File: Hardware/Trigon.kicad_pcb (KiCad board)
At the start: 2 copper layers, 160 x 120 mm, 110 parts, among them J1 TYPE-C-31-M12_13, J2 TYPE-C-31-M12_13, J3 Conn_01x05, SW1 SW_Push, SW2 Rotary_Encoder_Switch, U1 ATmega32U4-AU, U2 USBLC6-2SC6, U3 CY7C65632-28LTXCT, U4 USBLC6-2SC6, Y1 16MHz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

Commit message: minor tweaks to layout
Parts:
- moved C7 2.87 mm to (138.9, 59.5)
- moved C5 1.12 mm to (151.6, 61.9)
- moved C4 0.79 mm to (154.8, 48.4)
- moved R1 0.38 mm to (135.8, 55.2)
- moved R2 0.38 mm to (135.8, 56.8)
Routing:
- net COL6: track 22.3 -> 26.9 mm
- net D1_D-: track 57.4 -> 61.4 mm
- net GND: track 49.1 -> 46.3 mm
- net +5V: track 286.3 -> 288.7 mm, vias 9 -> 10
- net D1_D+: track 60.0 -> 61.5 mm

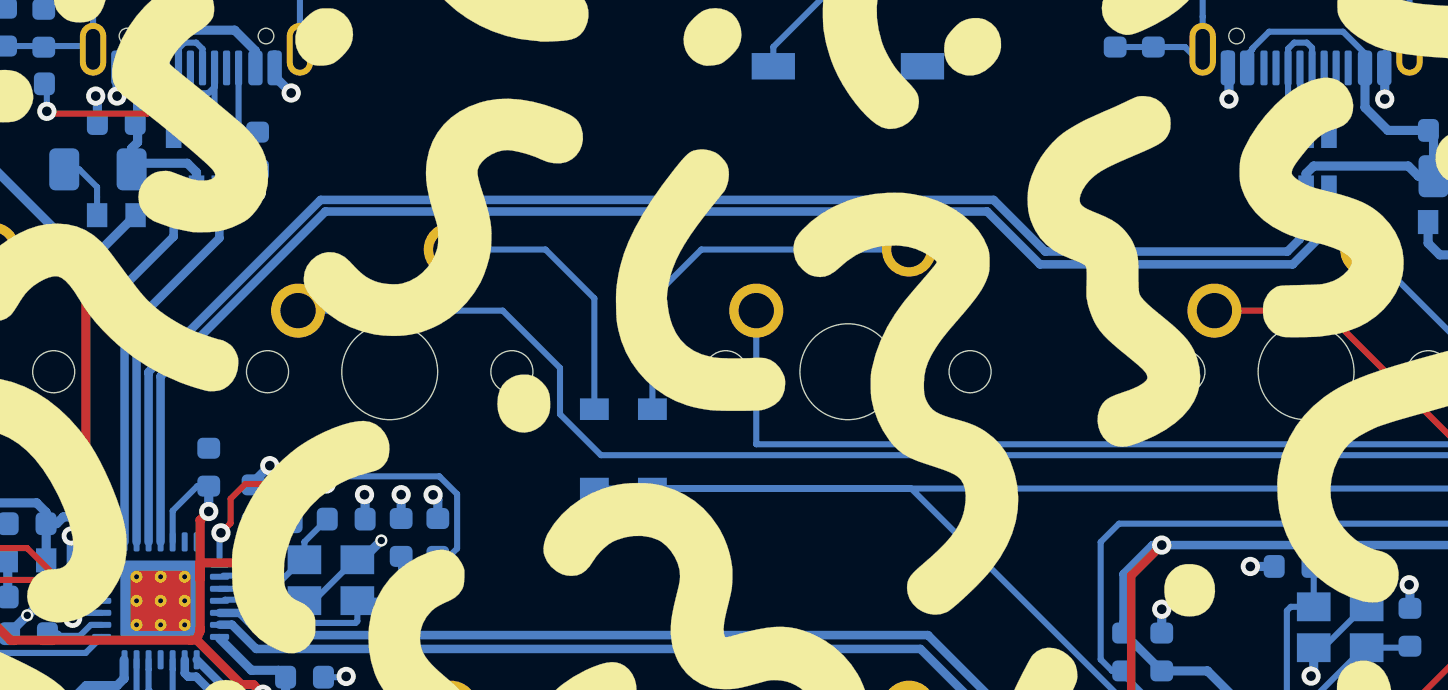
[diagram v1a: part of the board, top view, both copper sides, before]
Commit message: more space for usb
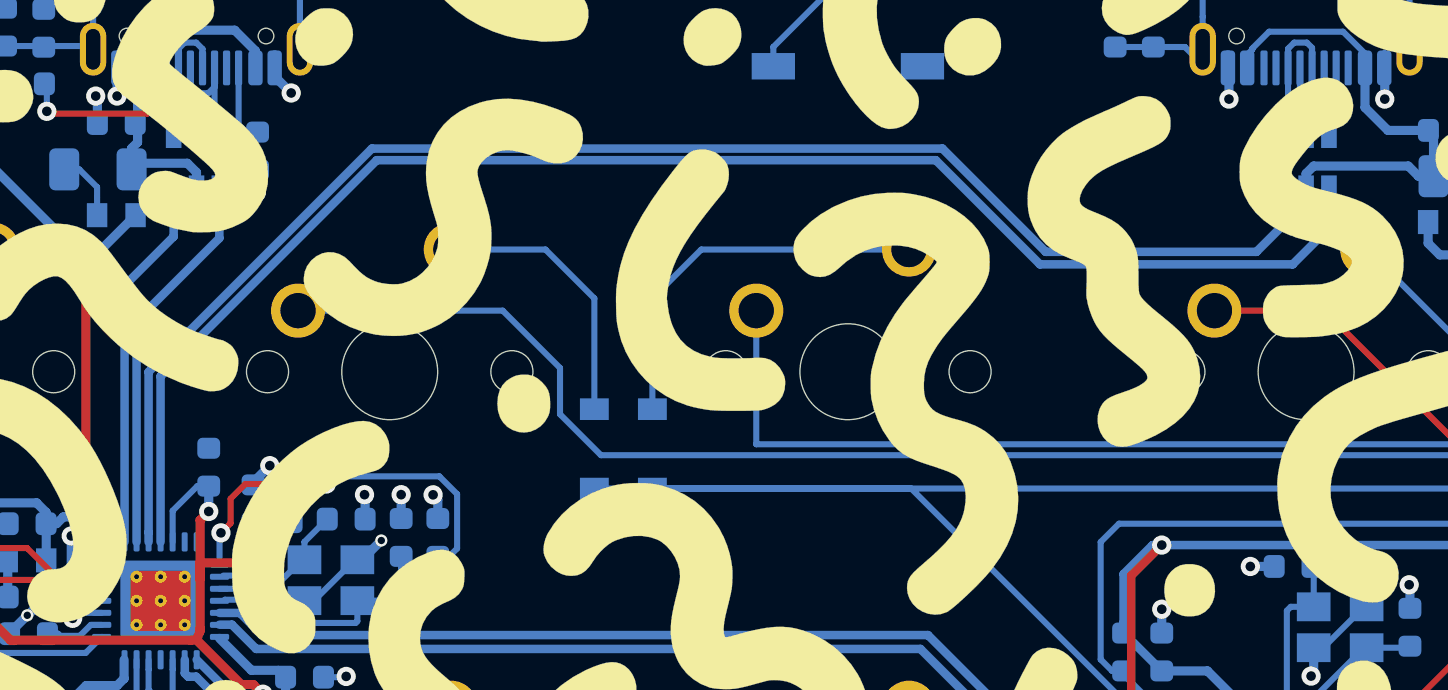
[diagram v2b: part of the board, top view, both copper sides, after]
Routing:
- net D1_D+: track 61.5 -> 63.3 mm
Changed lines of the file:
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@@
     (thickness 1.6)
     (drawings 21)
-    (tracks 814)
+    (tracks 812)
     (zones 0)
     (modules 110)
@@
   (segment (start 98.21875 30.43225) (end 101.661 26.99) (width 0.3556) (layer B.Cu) (net 97))
   (segment (start 98.21875 39.61875) (end 98.21875 30.43225) (width 0.3556) (layer B.Cu) (net 97))
-  (segment (start 146.57705 27.035778) (end 146.066528 27.5463) (width 0.3556) (layer B.Cu) (net 98))
-  (segment (start 98.71875 32.551737) (end 98.71875 32.59925) (width 0.3556) (layer B.Cu) (net 98))
-  (segment (start 98.71875 32.59925) (end 98.71875 39.61875) (width 0.3556) (layer B.Cu) (net 98))
-  (segment (start 146.066528 27.5463) (end 136.000472 27.5463) (width 0.3556) (layer B.Cu) (net 98))
-  (segment (start 105.870487 25.4) (end 98.71875 32.551737) (width 0.3556) (layer B.Cu) (net 98))
-  (segment (start 133.854172 25.4) (end 105.870487 25.4) (width 0.3556) (layer B.Cu) (net 98))
-  (segment (start 145.89375 24.9125) (end 145.89375 25.707501) (width 0.3556) (layer B.Cu) (net 98))
-  (segment (start 136.000472 27.5463) (end 133.854172 25.4) (width 0.3556) (layer B.Cu) (net 98))
-  (segment (start 145.89375 25.707501) (end 146.57705 26.390801) (width 0.3556) (layer B.Cu) (net 98))
-  (segment (start 146.57705 26.390801) (end 146.57705 27.035778) (width 0.3556) (layer B.Cu) (net 98))
-  (segment (start 135.779528 28.0797) (end 133.582439 25.882611) (width 0.3556) (layer B.Cu) (net 99))
+  (segment (start 98.71875 32.551736) (end 98.71875 39.21875) (width 0.3556) (layer B.Cu) (net 98))
+  (segment (start 98.71875 39.21875) (end 98.71875 39.61875) (width 0.3556) (layer B.Cu) (net 98))
+  (segment (start 108.004097 23.266389) (end 98.71875 32.551736) (width 0.3556) (layer B.Cu) (net 98))
+  (segment (start 131.724389 23.266389) (end 108.004097 23.266389) (width 0.3556) (layer B.Cu) (net 98))
+  (segment (start 136.017 27.559) (end 131.724389 23.266389) (width 0.3556) (layer B.Cu) (net 98))
+  (segment (start 145.89375 26.44525) (end 144.78 27.559) (width 0.3556) (layer B.Cu) (net 98))
+  (segment (start 144.78 27.559) (end 136.017 27.559) (width 0.3556) (layer B.Cu) (net 98))
+  (segment (start 145.89375 24.9125) (end 145.89375 26.44525) (width 0.3556) (layer B.Cu) (net 98))
   (segment (start 99.21594 32.737061) (end 99.21594 39.61875) (width 0.3556) (layer B.Cu) (net 99))
-  (segment (start 133.582439 25.882611) (end 106.07039 25.882611) (width 0.3556) (layer B.Cu) (net 99))
+  (segment (start 108.204001 23.749) (end 99.21594 32.737061) (width 0.3556) (layer B.Cu) (net 99))
+  (segment (start 135.779528 28.0797) (end 131.448828 23.749) (width 0.3556) (layer B.Cu) (net 99))
   (segment (start 147.79375 26.573422) (end 146.287472 28.0797) (width 0.3556) (layer B.Cu) (net 99))
   (segment (start 147.79375 24.9125) (end 147.79375 26.573422) (width 0.3556) (layer B.Cu) (net 99))
-  (segment (start 106.07039 25.882611) (end 99.21594 32.737061) (width 0.3556) (layer B.Cu) (net 99))
   (segment (start 146.287472 28.0797) (end 135.779528 28.0797) (width 0.3556) (layer B.Cu) (net 99))
+  (segment (start 131.448828 23.749) (end 108.204001 23.749) (width 0.3556) (layer B.Cu) (net 99))
   (segment (start 97.409 45.593) (end 97.70124 45.30076) (width 0.381) (layer B.Cu) (net 100))
   (segment (start 96.12125 45.593) (end 97.409 45.593) (width 0.381) (layer B.Cu) (net 100))

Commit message: min track width
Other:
- net class Narrow removed
- rule trace_min: 0.1524 -> 0.1778
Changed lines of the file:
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@@
   (setup
     (last_trace_width 0.254)
-    (user_trace_width 0.1524)
     (user_trace_width 0.2032)
     (user_trace_width 0.254)
@@
     (zone_clearance 0.25)
     (zone_45_only no)
-    (trace_min 0.1524)
+    (trace_min 0.1778)
     (via_size 0.8)
     (via_drill 0.4)
@@
     (add_net nOVR_4)
   )
-  (net_class Narrow ""
-    (clearance 0.127)
-    (trace_width 0.254)
-    (via_dia 0.8)
-    (via_drill 0.4)
-    (uvia_dia 0.3)
-    (uvia_drill 0.1)
-  )
   (net_class Power ""
     (clearance 0.2)
@@
   (segment (start 132.22175 16.14375) (end 132.334 16.256) (width 0.381) (layer B.Cu) (net 40))
   (segment (start 130.89375 16.14375) (end 132.22175 16.14375) (width 0.381) (layer B.Cu) (net 40))
-  (via (at 155.575 60.706) (size 0.8) (drill 0.4) (layers F.Cu B.Cu) (net 40))
-  (segment (start 155.575 59.74725) (end 155.575 60.706) (width 0.1524) (layer B.Cu) (net 40))
-  (via (at 149.352 41.148) (size 0.8) (drill 0.4) (layers F.Cu B.Cu) (net 40))
-  (segment (start 149.360417 41.156417) (end 149.352 41.148) (width 0.1524) (layer B.Cu) (net 40))
-  (segment (start 149.360417 42.317424) (end 149.360417 41.156417) (width 0.1524) (layer B.Cu) (net 40))
   (via (at 151.13 41.402) (size 0.8) (drill 0.4) (layers F.Cu B.Cu) (net 40))
   (via (at 140.843 42.418) (size 0.8) (drill 0.4) (layers F.Cu B.Cu) (net 40))
@@
   (segment (start 154.78125 46.76775) (end 154.813 46.736) (width 0.381) (layer B.Cu) (net 40))
   (segment (start 154.78125 47.63125) (end 154.78125 46.76775) (width 0.381) (layer B.Cu) (net 40))
+  (via (at 155.575 60.706) (size 0.8) (drill 0.4) (layers F.Cu B.Cu) (net 40))
+  (segment (start 155.575 59.74725) (end 155.575 60.706) (width 0.381) (layer B.Cu) (net 40))
+  (via (at 149.352 41.148) (size 0.8) (drill 0.4) (layers F.Cu B.Cu) (net 40))
+  (segment (start 149.360417 41.156417) (end 149.352 41.148) (width 0.381) (layer B.Cu) (net 40))
+  (segment (start 149.360417 42.317424) (end 149.360417 41.156417) (width 0.381) (layer B.Cu) (net 40))
   (segment (start 149.260417 44.017424) (end 149.360417 44.017424) (width 0.254) (layer B.Cu) (net 41))
   (segment (start 146.84375 46.434091) (end 149.260417 44.017424) (width 0.254) (layer B.Cu) (net 41))

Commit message: some via weirdness
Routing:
- net GND: track 46.3 -> 47.4 mm
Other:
- rule via_min_drill: 0.3 -> 0.4
- rule via_min_size: 0.4 -> 0.5
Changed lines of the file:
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@@
     (thickness 1.6)
     (drawings 21)
-    (tracks 812)
+    (tracks 814)
     (zones 0)
     (modules 110)
@@
     (via_size 0.8)
     (via_drill 0.4)
-    (via_min_size 0.4)
-    (via_min_drill 0.3)
-    (user_via 0.45 0.3048)
-    (user_via 0.508 0.3048)
+    (via_min_size 0.5)
+    (via_min_drill 0.4)
     (uvia_size 0.3)
     (uvia_drill 0.1)
     (uvias_allowed no)
-    (uvia_min_size 0.2)
+    (uvia_min_size 0.3)
     (uvia_min_drill 0.1)
     (edge_width 0.05)
@@
   (segment (start 110.744 38.646) (end 110.744 37.858134) (width 0.381) (layer B.Cu) (net 40))
   (segment (start 107.399 40.3615) (end 107.53 40.3615) (width 0.254) (layer B.Cu) (net 40))
-  (via (at 108.3945 39.5605) (size 0.508) (drill 0.3048) (layers F.Cu B.Cu) (net 40))
-  (segment (start 107.5935 40.3615) (end 108.3945 39.5605) (width 0.381) (layer B.Cu) (net 40))
-  (segment (start 107.399 40.3615) (end 107.5935 40.3615) (width 0.381) (layer B.Cu) (net 40))
   (via (at 105.283 36.322) (size 0.8) (drill 0.4) (layers F.Cu B.Cu) (net 40))
   (segment (start 104.648 36.957) (end 105.283 36.322) (width 0.381) (layer B.Cu) (net 40))
@@
   (segment (start 153.505 21.501) (end 153.543 21.463) (width 0.381) (layer B.Cu) (net 40))
   (segment (start 153.505 22.51075) (end 153.505 21.501) (width 0.381) (layer B.Cu) (net 40))
-  (via (at 93.6752 42.672) (size 0.508) (drill 0.3048) (layers F.Cu B.Cu) (net 40))
-  (segment (start 92.9385 43.4087) (end 93.6752 42.672) (width 0.381) (layer B.Cu) (net 40))
   (segment (start 92.9385 43.434) (end 92.9385 43.4087) (width 0.381) (layer B.Cu) (net 40))
-  (segment (start 93.69425 42.672) (end 94.45625 41.91) (width 0.381) (layer B.Cu) (net 40))
-  (segment (start 93.6752 42.672) (end 93.69425 42.672) (width 0.381) (layer B.Cu) (net 40))
   (via (at 132.334 16.256) (size 0.8) (drill 0.4) (layers F.Cu B.Cu) (net 40))
   (segment (start 132.22175 16.14375) (end 132.334 16.256) (width 0.381) (layer B.Cu) (net 40))
@@
   (segment (start 149.360417 41.156417) (end 149.352 41.148) (width 0.381) (layer B.Cu) (net 40))
   (segment (start 149.360417 42.317424) (end 149.360417 41.156417) (width 0.381) (layer B.Cu) (net 40))
+  (segment (start 104.0375 42.0615) (end 104.013 42.037) (width 0.381) (layer B.Cu) (net 40))
+  (via (at 104.013 42.037) (size 0.8) (drill 0.4) (layers F.Cu B.Cu) (net 40))
+  (segment (start 105.199 42.0615) (end 104.0375 42.0615) (width 0.381) (layer B.Cu) (net 40))
+  (segment (start 94.45625 41.91625) (end 92.9385 43.434) (width 0.381) (layer B.Cu) (net 40))
+  (segment (start 94.45625 41.91) (end 94.45625 41.91625) (width 0.381) (layer B.Cu) (net 40))
+  (segment (start 92.9385 43.434) (end 92.456 43.434) (width 0.381) (layer B.Cu) (net 40))
+  (segment (start 92.456 43.434) (end 92.347999 43.542001) (width 0.381) (layer B.Cu) (net 40))
+  (via (at 91.948 43.942) (size 0.8) (drill 0.4) (layers F.Cu B.Cu) (net 40))
+  (segment (start 92.347999 43.542001) (end 91.948 43.942) (width 0.381) (layer B.Cu) (net 40))
   (segment (start 149.260417 44.017424) (end 149.360417 44.017424) (width 0.254) (layer B.Cu) (net 41))
   (segment (start 146.84375 46.434091) (end 149.260417 44.017424) (width 0.254) (layer B.Cu) (net 41))
@@
   (segment (start 105.199 39.619) (end 106.1465 38.6715) (width 0.254) (layer B.Cu) (net 66))
   (segment (start 105.199 40.3615) (end 105.199 39.619) (width 0.254) (layer B.Cu) (net 66))
-  (segment (start 105.099 40.3615) (end 105.199 40.3615) (width 0.254) (layer B.Cu) (net 66))
-  (segment (start 103.89175 41.56875) (end 105.099 40.3615) (width 0.254) (layer B.Cu) (net 66))
-  (segment (start 101.66875 41.56875) (end 103.89175 41.56875) (width 0.254) (layer B.Cu) (net 66))
+  (segment (start 104.4185 40.3615) (end 105.199 40.3615) (width 0.254) (layer B.Cu) (net 66))
+  (segment (start 103.21125 41.56875) (end 104.4185 40.3615) (width 0.254) (layer B.Cu) (net 66))
+  (segment (start 101.66875 41.56875) (end 103.21125 41.56875) (width 0.254) (layer B.Cu) (net 66))
   (segment (start 109.22 41.1945) (end 109.22 40.6585) (width 0.254) (layer B.Cu) (net 67))
   (segment (start 108.353 42.0615) (end 109.22 41.1945) (width 0.254) (layer B.Cu) (net 67))
@@
   (segment (start 107.399 42.0615) (end 108.353 42.0615) (width 0.254) (layer B.Cu) (net 67))
   (segment (start 107.399 42.9155) (end 107.399 42.0615) (width 0.254) (layer B.Cu) (net 67))
+  (segment (start 103.821501 42.988501) (end 107.325999 42.988501) (width 0.254) (layer B.Cu) (net 67))
   (segment (start 107.325999 42.988501) (end 107.399 42.9155) (width 0.254) (layer B.Cu) (net 67))
-  (segment (start 104.237399 42.988501) (end 107.325999 42.988501) (width 0.254) (layer B.Cu) (net 67))
-  (segment (start 101.89364 42.02276) (end 103.271658 42.02276) (width 0.254) (layer B.Cu) (net 67))
-  (segment (start 103.271658 42.02276) (end 104.237399 42.988501) (width 0.254) (layer B.Cu) (net 67))
+  (segment (start 102.85576 42.02276) (end 103.821501 42.988501) (width 0.254) (layer B.Cu) (net 67))
+  (segment (start 101.89364 42.02276) (end 102.85576 42.02276) (width 0.254) (layer B.Cu) (net 67))
   (segment (start 101.8794 42.037) (end 101.89364 42.02276) (width 0.254) (layer B.Cu) (net 67))
   (segment (start 97.65675 48.54575) (end 97.663 48.54575) (width 0.381) (layer B.Cu) (net 68))
@@
   (segment (start 103.14526 40.49174) (end 103.886 39.751) (width 0.381) (layer F.Cu) (net 69))
   (segment (start 100.85926 40.49174) (end 103.14526 40.49174) (width 0.381) (layer F.Cu) (net 69))
-  (segment (start 92.456 41.91) (end 91.821 42.545) (width 0.381) (layer B.Cu) (net 69))
-  (via (at 91.821 42.545) (size 0.8) (drill 0.4) (layers F.Cu B.Cu) (net 69))
-  (segment (start 92.88125 41.91) (end 92.456 41.91) (width 0.381) (layer B.Cu) (net 69))
-  (segment (start 91.821 42.545) (end 91.948 42.545) (width 0.381) (layer F.Cu) (net 69))
   (segment (start 100.85926 43.33406) (end 100.85926 43.20126) (width 0.381) (layer F.Cu) (net 69))
   (via (at 103.474901 45.951733) (size 0.8) (drill 0.4) (layers F.Cu B.Cu) (net 69))
@@
   (segment (start 104.414883 45.243751) (end 104.129132 44.958) (width 0.381) (layer B.Cu) (net 69))
   (segment (start 104.414883 46.76775) (end 104.414883 45.243751) (width 0.381) (layer B.Cu) (net 69))
-  (segment (start 100.48406 43.70926) (end 100.711 43.688) (width 0.381) (layer F.Cu) (net 69))
-  (segment (start 92.98526 43.70926) (end 100.48406 43.70926) (width 0.381) (layer F.Cu) (net 69))
-  (segment (start 91.821 42.545) (end 92.98526 43.70926) (width 0.381) (layer F.Cu) (net 69))
   (segment (start 99.72075 38.32325) (end 99.72075 39.61875) (width 0.254) (layer B.Cu) (net 69))
   (segment (start 100.744 37.3) (end 99.72075 38.32325) (width 0.254) (layer B.Cu) (net 69))
@@
   (segment (start 103.0605 38.824) (end 103.0605 40.41976) (width 0.381) (layer B.Cu) (net 69))
   (segment (start 103.0605 40.41976) (end 102.45926 41.021) (width 0.381) (layer B.Cu) (net 69))
+  (segment (start 92.329 41.91) (end 91.694 42.545) (width 0.381) (layer B.Cu) (net 69))
+  (segment (start 92.88125 41.91) (end 92.329 41.91) (width 0.381) (layer B.Cu) (net 69))
+  (segment (start 100.48406 43.70926) (end 92.85826 43.70926) (width 0.381) (layer F.Cu) (net 69))
+  (segment (start 100.711 43.688) (end 100.48406 43.70926) (width 0.381) (layer F.Cu) (net 69))
+  (segment (start 92.093999 42.944999) (end 91.694 42.545) (width 0.381) (layer F.Cu) (net 69))
+  (segment (start 92.85826 43.70926) (end 92.093999 42.944999) (width 0.381) (layer F.Cu) (net 69))
+  (via (at 91.694 42.545) (size 0.8) (drill 0.4) (layers F.Cu B.Cu) (net 69))
   (segment (start 149.29375 19.318972) (end 149.29375 19.3625) (width 0.254) (layer B.Cu) (net 70))
   (segment (start 145.306242 18.40648) (end 148.381258 18.40648) (width 0.254) (layer B.Cu) (net 70))
@@
   (segment (start 102.51556 42.57156) (end 101.66875 42.57156) (width 0.3556) (layer B.Cu) (net 73))
   (segment (start 131.123311 43.493311) (end 103.437311 43.493311) (width 0.3556) (layer B.Cu) (net 73))
-  (segment (start 90.30026 44.23601) (end 89.08425 43.02) (width 0.254) (layer B.Cu) (net 74))
-  (segment (start 96.76875 43.56875) (end 96.10149 44.23601) (width 0.254) (layer B.Cu) (net 74))
-  (segment (start 96.10149 44.23601) (end 90.30026 44.23601) (width 0.254) (layer B.Cu) (net 74))
+  (segment (start 96.76875 43.56875) (end 95.668498 44.669002) (width 0.254) (layer B.Cu) (net 74))
+  (segment (start 90.733252 44.669002) (end 89.08425 43.02) (width 0.254) (layer B.Cu) (net 74))
   (segment (start 89.08425 43.02) (end 89.08425 42.545) (width 0.254) (layer B.Cu) (net 74))
+  (segment (start 95.668498 44.669002) (end 90.733252 44.669002) (width 0.254) (layer B.Cu) (net 74))
   (segment (start 95.862514 43.524134) (end 96.317898 43.06875) (width 0.254) (layer B.Cu) (net 75))
   (segment (start 95.041134 43.524134) (end 95.862514 43.524134) (width 0.254) (layer B.Cu) (net 75))
